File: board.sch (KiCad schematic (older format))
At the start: 32 parts, among them J0 Battery Pads, J1 Shard, J2 USB-Micro, SW0 RESET, SW1 UP, SW2 DOWN, SW3 LEFT, SW4 RIGHT, SW5 BTN_A, SW6 BTN_B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

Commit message: board revised for mono oled
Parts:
- removed C4: 1uF, Capacitor_THT:C_Rect_L7.0mm_W2.5mm_P5.00mm, symbol Device:C
- removed R2, R3, R4, R5, R6, R7: 1K, Resistor_THT:R_Axial_DIN0207_L6.3mm_D2.5mm_P7.62mm_Horizontal, symbol Device:R
- removed R9: 10k, Resistor_THT:R_Axial_DIN0207_L6.3mm_D2.5mm_P7.62mm_Horizontal, symbol Device:R
- added D1: CHG, LED_THT:LED_D3.0mm, symbol Device:LED_ALT
- C1: value 1uF -> 104
- C2, C3: value 1uF -> 105
- C5, C6: value 4.7uF -> 475
- R1: value 1K -> LED
- U1: footprint Custom Footprints:128x128-OLED -> Custom Footprints:128x64-OLED
- U2: value CHG -> CHG CTRL
- renumbered R8 to R2
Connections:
- wire segments 93 -> 81
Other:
- moved on the sheet: C5, C6, J2, R2, U2

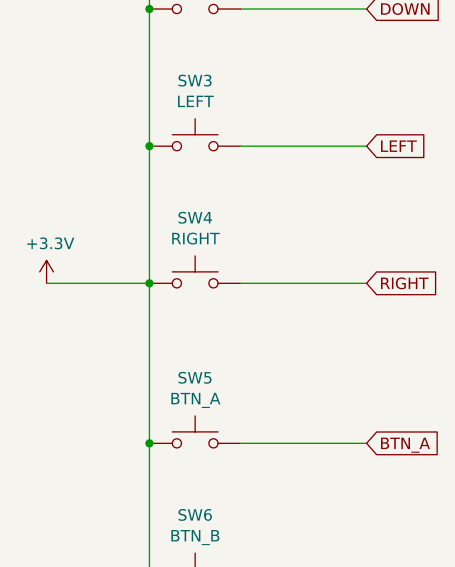
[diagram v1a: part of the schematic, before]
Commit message: swapped buttons to pull to GND
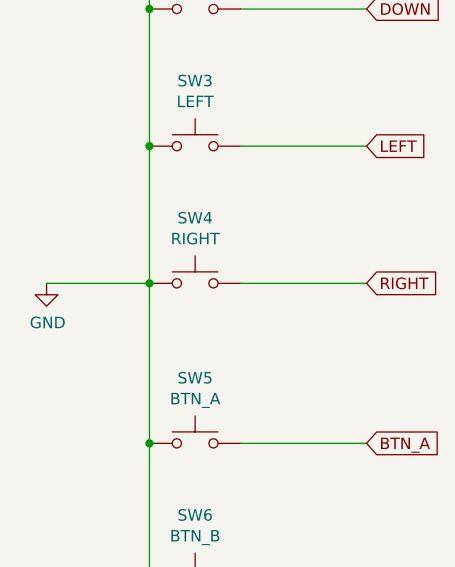
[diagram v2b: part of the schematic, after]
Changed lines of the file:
@@
-	1    0    0    -1
-$EndComp
-$Comp
-L power:+3.3V #PWR01
-U 1 1 5BACB3A5
-P 700 4000
-F 0 "#PWR01" H 700 3850 50  0001 C CNN
-F 1 "+3.3V" H 715 4173 50  0000 C CNN
-F 2 "" H 700 4000 50  0001 C CNN
-F 3 "" H 700 4000 50  0001 C CNN
-	1    700  4000
 	1    0    0    -1
 $EndComp
@@
 Wire Wire Line
 	6100 2900 6250 2900
+$Comp
+L power:GND #PWR?
+U 1 1 5BEB806B
+P 700 4000
+F 0 "#PWR?" H 700 3750 50  0001 C CNN
+F 1 "GND" H 705 3827 50  0000 C CNN
+F 2 "" H 700 4000 50  0001 C CNN
+F 3 "" H 700 4000 50  0001 C CNN
+	1    700  4000
+	1    0    0    -1
+$EndComp
 $EndSCHEMATC

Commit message: Edge Connector for Shards
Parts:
- removed J1: Shard, Connector_PinHeader_2.54mm:PinHeader_2x10_P2.54mm_Vertical, symbol Connector_Generic:Conn_02x10_Odd_Even
- added J1: Shard, Connector_PCBEdge:Samtec_MECF-20-01-NP-L-DV-WT_2x20_P1.27mm_Socket_Horizontal, symbol Connector_Generic:Conn_02x20_Odd_Even
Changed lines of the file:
@@
 Text GLabel 2050 1500 2    50   Input ~ 0
 RESET
-Text GLabel 5450 2600 0    50   Input ~ 0
+Text GLabel 7400 2300 2    50   Input ~ 0
 RESET
 $Comp
 L power:+3.3V #PWR022
 U 1 1 5BAD1FC0
-P 5450 2200
-F 0 "#PWR022" H 5450 2050 50  0001 C CNN
-F 1 "+3.3V" H 5465 2373 50  0000 C CNN
-F 2 "" H 5450 2200 50  0001 C CNN
-F 3 "" H 5450 2200 50  0001 C CNN
-	1    5450 2200
-	1    0    0    -1
-$EndComp
-Text GLabel 5450 2700 0    50   Input ~ 0
+P 7400 1550
+F 0 "#PWR022" H 7400 1400 50  0001 C CNN
+F 1 "+3.3V" H 7415 1723 50  0000 C CNN
+F 2 "" H 7400 1550 50  0001 C CNN
+F 3 "" H 7400 1550 50  0001 C CNN
+	1    7400 1550
+	1    0    0    -1
+$EndComp
+Text GLabel 7400 3100 2    50   Input ~ 0
 UP
-Text GLabel 5450 3000 0    50   Input ~ 0
+Text GLabel 7400 3200 2    50   Input ~ 0
 DOWN
-Text GLabel 5450 2900 0    50   Input ~ 0
+Text GLabel 7400 3300 2    50   Input ~ 0
 LEFT
-Text GLabel 5450 2800 0    50   Input ~ 0
+Text GLabel 7400 3400 2    50   Input ~ 0
 RIGHT
-Text GLabel 5450 2300 0    50   Input ~ 0
+Text GLabel 7400 1900 2    50   Input ~ 0
 BTN_A
-Text GLabel 5450 2400 0    50   Input ~ 0
+Text GLabel 7400 2000 2    50   Input ~ 0
 BTN_B
-Text GLabel 5450 2500 0    50   Input ~ 0
+Text GLabel 7400 2100 2    50   Input ~ 0
 BTN_C
 Text GLabel 2100 2200 2    50   Input ~ 0
@@
 Text GLabel 2150 6950 2    50   Input ~ 0
 SND
-Text GLabel 6250 3000 2    50   Input ~ 0
+Text GLabel 7400 3000 2    50   Input ~ 0
 SND
 Wire Wire Line
@@
 Wire Wire Line
 	6000 4150 6000 4300
-Text GLabel 6250 2700 2    50   Input ~ 0
+Text GLabel 7400 2700 2    50   Input ~ 0
 D_RST
 Text GLabel 6100 4150 1    50   Input ~ 0
@@
 Wire Wire Line
 	6100 4150 6100 4300
-Text GLabel 6250 2600 2    50   Input ~ 0
+Text GLabel 7400 2600 2    50   Input ~ 0
 D_DC
 Text GLabel 6200 4150 1    50   Input ~ 0
@@
 Wire Wire Line
 	6200 4150 6200 4300
-Text GLabel 6250 2500 2    50   Input ~ 0
+Text GLabel 7400 2500 2    50   Input ~ 0
 D_CS
 $Comp
@@
 Wire Wire Line
 	5400 4300 5600 4300
-Text GLabel 6250 2900 2    50   Input ~ 0
+Text GLabel 7400 2900 2    50   Input ~ 0
 D_SCK
 Text GLabel 5800 4150 1    50   Input ~ 0
 D_SCK
-Text GLabel 6250 2800 2    50   Input ~ 0
+Text GLabel 7400 2800 2    50   Input ~ 0
 D_MOSI
 Text GLabel 5900 4150 1    50   Input ~ 0
@@
 Wire Wire Line
 	3850 5500 4000 5500
-Text GLabel 6250 2400 2    50   Input ~ 0
+Text GLabel 7400 1800 2    50   Input ~ 0
 D+
-Text GLabel 6250 2300 2    50   Input ~ 0
+Text GLabel 7400 1700 2    50   Input ~ 0
 D-
-$Comp
-L Connector_Generic:Conn_02x10_Odd_Even J1
-U 1 1 5BD94B77
-P 5800 2600
-F 0 "J1" H 5850 3217 50  0000 C CNN
-F 1 "Shard" H 5850 3126 50  0000 C CNN
-F 2 "Connector_PinHeader_2.54mm:PinHeader_2x10_P2.54mm_Vertical" H 5800 2600 50  0001 C CNN
-F 3 "~" H 5800 2600 50  0001 C CNN
-	1    5800 2600
-	1    0    0    -1
-$EndComp
 Wire Wire Line
 	2050 7050 2050 7250
-Wire Wire Line
-	5450 2200 5600 2200
-Wire Wire Line
-	5450 2300 5600 2300
-Wire Wire Line
-	5450 2400 5600 2400
-Wire Wire Line
-	5600 2500 5450 2500
-Wire Wire Line
-	5450 2600 5600 2600
-Wire Wire Line
-	5450 2800 5600 2800
-Wire Wire Line
-	5450 2900 5600 2900
-Wire Wire Line
-	6100 2300 6250 2300
-Wire Wire Line
-	6100 2400 6250 2400
-Wire Wire Line
-	6100 2500 6250 2500
-Wire Wire Line
-	6100 2600 6250 2600
 $Comp
 L power:+3.3V #PWR0101
@@
 Wire Wire Line
 	1850 950  1850 1100
-$Comp
-L power:GND #PWR0103
-U 1 1 5BE149B1
-P 6650 2200
-F 0 "#PWR0103" H 6650 1950 50  0001 C CNN
-F 1 "GND" H 6655 2027 50  0000 C CNN
-F 2 "" H 6650 2200 50  0001 C CNN
-F 3 "" H 6650 2200 50  0001 C CNN
-	1    6650 2200
-	1    0    0    -1
-$EndComp
-Wire Wire Line
-	5450 3000 5600 3000
-Wire Wire Line
-	6100 3000 6250 3000
-Wire Wire Line
-	5450 2700 5600 2700
 Wire Wire Line
 	1950 6950 2150 6950
@@
 Wire Wire Line
 	1550 5900 2100 5900
-Wire Wire Line
-	6100 2700 6250 2700
 $Comp
 L power:GND #PWR0104
-U 1 1 5BECACC3
-P 5350 3100
-F 0 "#PWR0104" H 5350 2850 50  0001 C CNN
-F 1 "GND" H 5355 2927 50  0000 C CNN
-F 2 "" H 5350 3100 50  0001 C CNN
-F 3 "" H 5350 3100 50  0001 C CNN
-	1    5350 3100
-	1    0    0    -1
-$EndComp
-Wire Wire Line
-	5350 3100 5600 3100
-Wire Wire Line
-	6100 2200 6650 2200
-$Comp
-L power:+3.3V #PWR0105
-U 1 1 5BECFF14
-P 6600 3100
-F 0 "#PWR0105" H 6600 2950 50  0001 C CNN
-F 1 "+3.3V" H 6615 3273 50  0000 C CNN
-F 2 "" H 6600 3100 50  0001 C CNN
-F 3 "" H 6600 3100 50  0001 C CNN
-	1    6600 3100
-	1    0    0    -1
-$EndComp
-Wire Wire Line
-	6100 3100 6600 3100
-Wire Wire Line
-	6100 2800 6250 2800
-Wire Wire Line
-	6100 2900 6250 2900
-$Comp
-L power:GND #PWR?
 U 1 1 5BEB806B
 P 700 4000
-F 0 "#PWR?" H 700 3750 50  0001 C CNN
+F 0 "#PWR0104" H 700 3750 50  0001 C CNN
 F 1 "GND" H 705 3827 50  0000 C CNN
 F 2 "" H 700 4000 50  0001 C CNN
@@
 	1    0    0    -1
 $EndComp
+$Comp
+L Connector_Generic:Conn_02x20_Odd_Even J1
+U 1 1 5BE9C917
+P 6950 2500
+F 0 "J1" H 7000 3617 50  0000 C CNN
+F 1 "Shard" H 7000 3526 50  0000 C CNN
+F 2 "Connector_PCBEdge:Samtec_MECF-20-01-NP-L-DV-WT_2x20_P1.27mm_Socket_Horizontal" H 6950 2500 50  0001 C CNN
+F 3 "~" H 6950 2500 50  0001 C CNN
+	1    6950 2500
+	1    0    0    -1
+$EndComp
+$Comp
+L power:GND #PWR0103
+U 1 1 5BE149B1
+P 7400 3550
+F 0 "#PWR0103" H 7400 3300 50  0001 C CNN
+F 1 "GND" H 7405 3377 50  0000 C CNN
+F 2 "" H 7400 3550 50  0001 C CNN
+F 3 "" H 7400 3550 50  0001 C CNN
+	1    7400 3550
+	1    0    0    -1
+$EndComp
+Wire Wire Line
+	7250 1600 7400 1600
+Wire Wire Line
+	7400 1600 7400 1550
+Wire Wire Line
+	7400 1700 7250 1700
+Wire Wire Line
+	7400 1800 7250 1800
+Wire Wire Line
+	7250 1900 7400 1900
+Wire Wire Line
+	7400 2000 7250 2000
+Wire Wire Line
+	7250 2100 7400 2100
+Wire Wire Line
+	7400 2300 7250 2300
+Wire Wire Line
+	7400 2500 7250 2500
+Wire Wire Line
+	7400 2600 7250 2600
+Wire Wire Line
+	7250 2700 7400 2700
+Wire Wire Line
+	7400 2800 7250 2800
+Wire Wire Line
+	7250 2900 7400 2900
+Wire Wire Line
+	7400 3000 7250 3000
+Wire Wire Line
+	7250 3100 7400 3100
+Wire Wire Line
+	7400 3200 7250 3200
+Wire Wire Line
+	7250 3300 7400 3300
+Wire Wire Line
+	7400 3400 7250 3400
+Wire Wire Line
+	7250 3500 7400 3500
+Wire Wire Line
+	7400 3500 7400 3550
 $EndSCHEMATC

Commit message: Board updated to edge connector
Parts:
- J1: footprint Connector_PCBEdge:Samtec_MECF-20-01-NP-L-DV-WT_2x20_P1.27mm_Socket_Horizontal -> Custom Footprints:Samtec_MEC8-120-02-L-D-RA1_Socket
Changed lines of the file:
@@
 F 0 "J1" H 7000 3617 50  0000 C CNN
 F 1 "Shard" H 7000 3526 50  0000 C CNN
-F 2 "Connector_PCBEdge:Samtec_MECF-20-01-NP-L-DV-WT_2x20_P1.27mm_Socket_Horizontal" H 6950 2500 50  0001 C CNN
+F 2 "Custom Footprints:Samtec_MEC8-120-02-L-D-RA1_Socket" H 6950 2500 50  0001 C CNN
 F 3 "~" H 6950 2500 50  0001 C CNN
 	1    6950 2500
